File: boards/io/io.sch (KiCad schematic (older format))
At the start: 129 parts, among them J1 61304021021, J2 SSW-120-02-G-D-RA, J3 Conn_01x09, J4 Barrel_Jack_Switch, J5 Conn_01x09, J6 SSW-120-02-G-D-RA, Q1 Q_NMOS_DGS, U1 SN74ACT32PWR, U10 74HC151, U11 MC74AC273DTR2G, U12 74LS32, U13 CY62256NLL-55ZXI, U14 74LS32, U2 74LS30, U3 74ACT00MTCX, U4 AT28C256-PLCC32, U5 CY62256NLL-55ZXI, U6 SSW-116-01-T-S, U7 MC74AC273DTR2G, U8 SN74ACT244PW, U9 74LS30

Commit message: IO board: device refs and datasheet links
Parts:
- removed Q1: Q_NMOS_DGS, symbol Device:Q_NMOS_DGS
- added Q1: 2N7002, Package_TO_SOT_SMD:SOT-23, symbol Device:Q_NMOS_GSD
- J4: value Barrel_Jack_Switch -> 694106301002
- U10: value 74HC151 -> MC74HC151ADTR2G; footprint (none) -> Package_SO:TSSOP-16_4.4x5mm_P0.65mm
- U12, U14: value 74LS32 -> SN74ACT32PWR; footprint (none) -> Package_SO:TSSOP-14_4.4x5mm_P0.65mm
- U13, U5: value CY62256NLL-55ZXI -> IS61C256AL-12TLI
- U2, U9: value 74LS30 -> 74HC30D; footprint (none) -> Package_SO:SOIC-14_3.9x8.7mm_P1.27mm
- gave numbers to parts that had none: 20

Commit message: Make n_rdy an open-drain pull-up
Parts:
- removed C13: 0.1u, Capacitor_SMD:C_0805_2012Metric, symbol Device:C
- removed Q1: 2N7002, Package_TO_SOT_SMD:SOT-23, symbol Device:Q_NMOS_GSD
- removed U2: 74HC30D, Package_SO:SOIC-14_3.9x8.7mm_P1.27mm, symbol 74xx:74LS30
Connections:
- wire segments 150 -> 142
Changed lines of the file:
@@
 NoConn ~ 8650 14450
 NoConn ~ 3900 7950
-$Comp
-L 74xx:74LS30 U2
-U 1 1 603249A4
-P 15500 9450
-F 0 "U2" H 15500 9975 50  0000 C CNN
-F 1 "74HC30D" H 15500 9884 50  0000 C CNN
-F 2 "Package_SO:SOIC-14_3.9x8.7mm_P1.27mm" H 15500 9450 50  0001 C CNN
-F 3 "https://assets.nexperia.com/documents/data-sheet/74HC_HCT30.pdf" H 15500 9450 50  0001 C CNN
-	1    15500 9450
-	1    0    0    -1
-$EndComp
-$Comp
-L 74xx:74LS30 U2
-U 2 1 60326108
-P 7100 14100
-F 0 "U2" H 7330 14146 50  0000 L CNN
-F 1 "74HC30D" H 7330 14055 50  0000 L CNN
-F 2 "Package_SO:SOIC-14_3.9x8.7mm_P1.27mm" H 7100 14100 50  0001 C CNN
-F 3 "https://assets.nexperia.com/documents/data-sheet/74HC_HCT30.pdf" H 7100 14100 50  0001 C CNN
-	2    7100 14100
-	1    0    0    -1
-$EndComp
-$Comp
-L power:GND #PWR095
-U 1 1 60326F40
-P 7100 14600
-F 0 "#PWR095" H 7100 14350 50  0001 C CNN
-F 1 "GND" H 7105 14427 50  0000 C CNN
-F 2 "" H 7100 14600 50  0001 C CNN
-F 3 "" H 7100 14600 50  0001 C CNN
-	1    7100 14600
-	1    0    0    -1
-$EndComp
-$Comp
-L power:VCC #PWR094
-U 1 1 60327344
-P 7100 13600
-F 0 "#PWR094" H 7100 13450 50  0001 C CNN
-F 1 "VCC" H 7117 13773 50  0000 C CNN
-F 2 "" H 7100 13600 50  0001 C CNN
-F 3 "" H 7100 13600 50  0001 C CNN
-	1    7100 13600
-	1    0    0    -1
-$EndComp
-Text Label 15200 9350 2    50   ~ 0
-~rom_cs
-Text Label 15200 9450 2    50   ~ 0
-~raml_cs
-Text Label 15200 9550 2    50   ~ 0
-~ramh_cs
-Text Label 15200 9650 2    50   ~ 0
-~io_cs
-$Comp
-L power:VCC #PWR0100
-U 1 1 6032E8ED
-P 15100 9050
-F 0 "#PWR0100" H 15100 8900 50  0001 C CNN
-F 1 "VCC" H 15117 9223 50  0000 C CNN
-F 2 "" H 15100 9050 50  0001 C CNN
-F 3 "" H 15100 9050 50  0001 C CNN
-	1    15100 9050
-	1    0    0    -1
-$EndComp
-Wire Wire Line
-	15200 9250 15100 9250
-Wire Wire Line
-	15100 9250 15100 9150
-Wire Wire Line
-	15200 9150 15100 9150
-Connection ~ 15100 9150
-Wire Wire Line
-	15100 9150 15100 9050
-$Comp
-L power:VCC #PWR0103
-U 1 1 60342DDE
-P 15100 9950
-F 0 "#PWR0103" H 15100 9800 50  0001 C CNN
-F 1 "VCC" H 15117 10123 50  0000 C CNN
-F 2 "" H 15100 9950 50  0001 C CNN
-F 3 "" H 15100 9950 50  0001 C CNN
-	1    15100 9950
-	-1   0    0    1
-$EndComp
-Wire Wire Line
-	15200 9750 15100 9750
-Wire Wire Line
-	15100 9750 15100 9850
-Wire Wire Line
-	15200 9850 15100 9850
-Connection ~ 15100 9850
-Wire Wire Line
-	15100 9850 15100 9950
-$Comp
-L power:GND #PWR0106
-U 1 1 6036BCCA
-P 16100 9650
-F 0 "#PWR0106" H 16100 9400 50  0001 C CNN
-F 1 "GND" H 16105 9477 50  0000 C CNN
-F 2 "" H 16100 9650 50  0001 C CNN
-F 3 "" H 16100 9650 50  0001 C CNN
-	1    16100 9650
-	1    0    0    -1
-$EndComp
-Text Label 16100 9250 2    50   ~ 0
-~rdy
 Wire Notes Line
 	16850 7350 16850 11600
@@
 	1    0    0    -1
 $EndComp
-$Comp
-L Device:C C13
-U 1 1 603D7405
-P 7150 15300
-F 0 "C13" H 7265 15346 50  0000 L CNN
-F 1 "0.1u" H 7265 15255 50  0000 L CNN
-F 2 "Capacitor_SMD:C_0805_2012Metric" H 7188 15150 50  0001 C CNN
-F 3 "~" H 7150 15300 50  0001 C CNN
-	1    7150 15300
-	1    0    0    -1
-$EndComp
-$Comp
-L power:GND #PWR0117
-U 1 1 603D740B
-P 7150 15450
-F 0 "#PWR0117" H 7150 15200 50  0001 C CNN
-F 1 "GND" H 7155 15277 50  0000 C CNN
-F 2 "" H 7150 15450 50  0001 C CNN
-F 3 "" H 7150 15450 50  0001 C CNN
-	1    7150 15450
-	1    0    0    -1
-$EndComp
-$Comp
-L power:VCC #PWR0116
-U 1 1 603D7411
-P 7150 15150
-F 0 "#PWR0116" H 7150 15000 50  0001 C CNN
-F 1 "VCC" H 7167 15323 50  0000 C CNN
-F 2 "" H 7150 15150 50  0001 C CNN
-F 3 "" H 7150 15150 50  0001 C CNN
-	1    7150 15150
-	1    0    0    -1
-$EndComp
 Wire Bus Line
 	17000 3250 17000 4100
@@
 Wire Bus Line
 	9350 1200 9350 2600
-$Comp
-L Device:Q_NMOS_GSD Q1
-U 1 1 603E8383
-P 16000 9450
-F 0 "Q1" H 16204 9496 50  0000 L CNN
-F 1 "2N7002" H 16204 9405 50  0000 L CNN
-F 2 "Package_TO_SOT_SMD:SOT-23" H 16200 9550 50  0001 C CNN
-F 3 "~" H 16000 9450 50  0001 C CNN
-	1    16000 9450
-	1    0    0    -1
-$EndComp
 $EndSCHEMATC

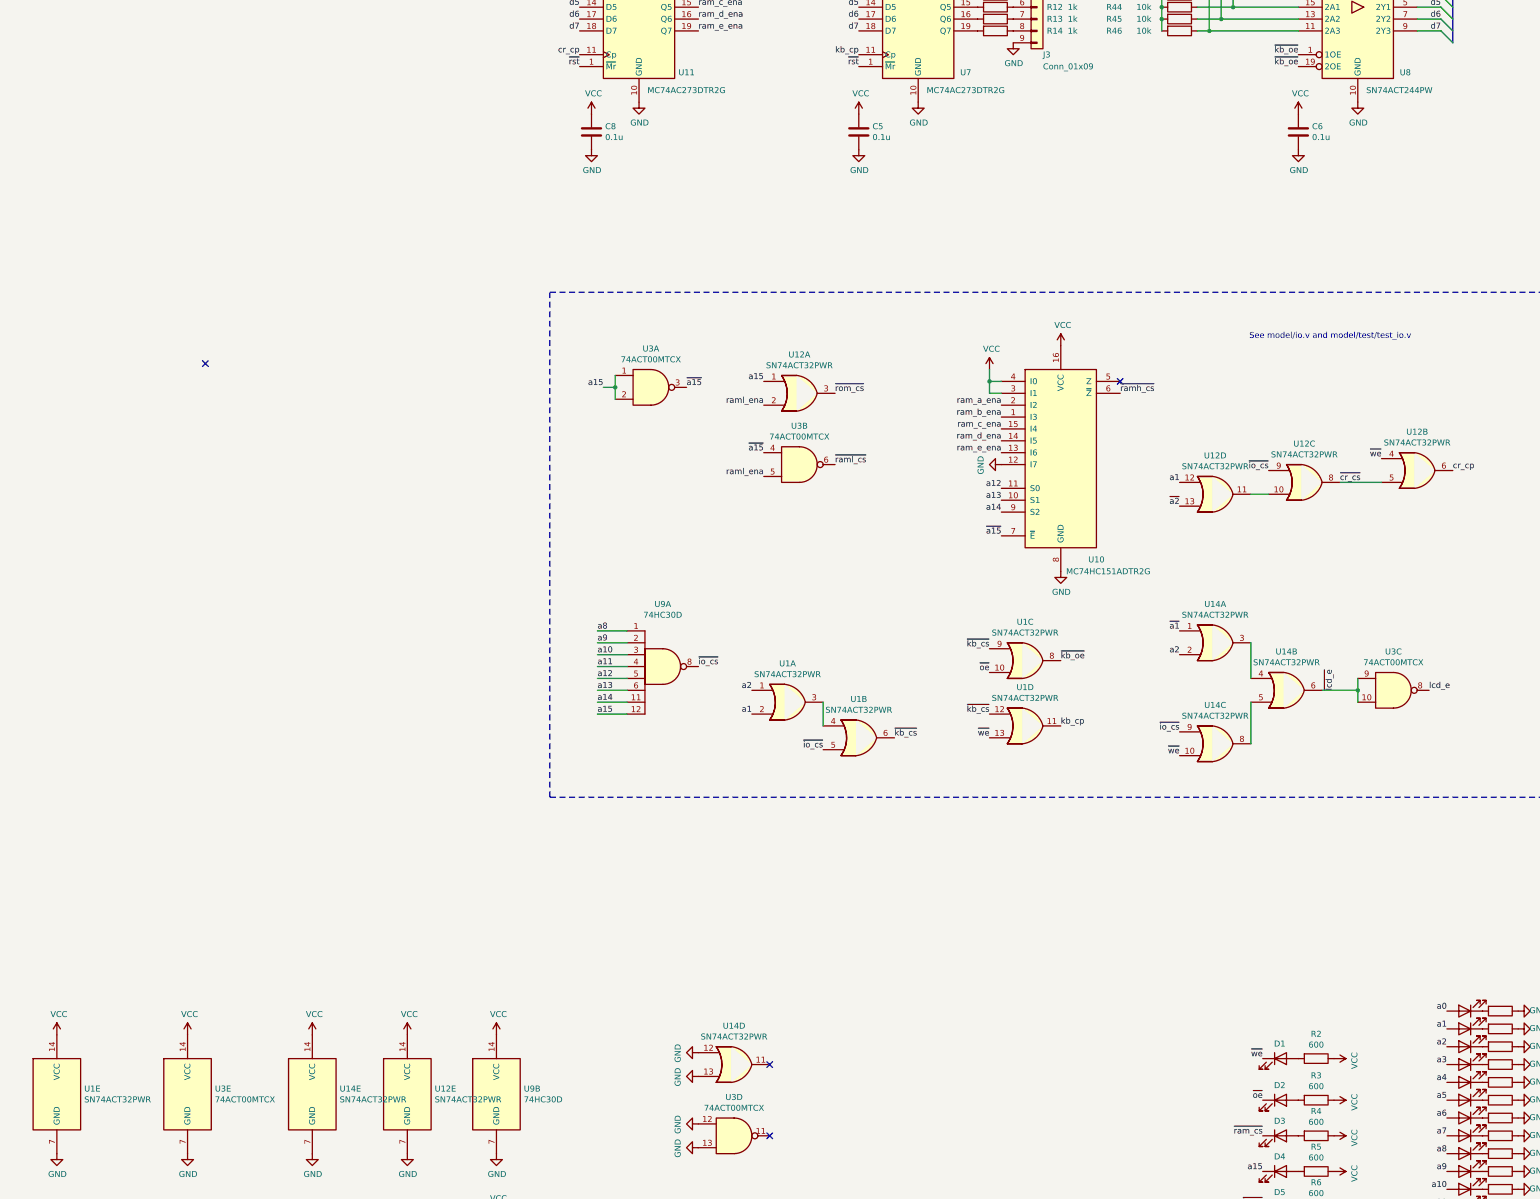
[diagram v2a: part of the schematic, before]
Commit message: IO: get rid of 74AC
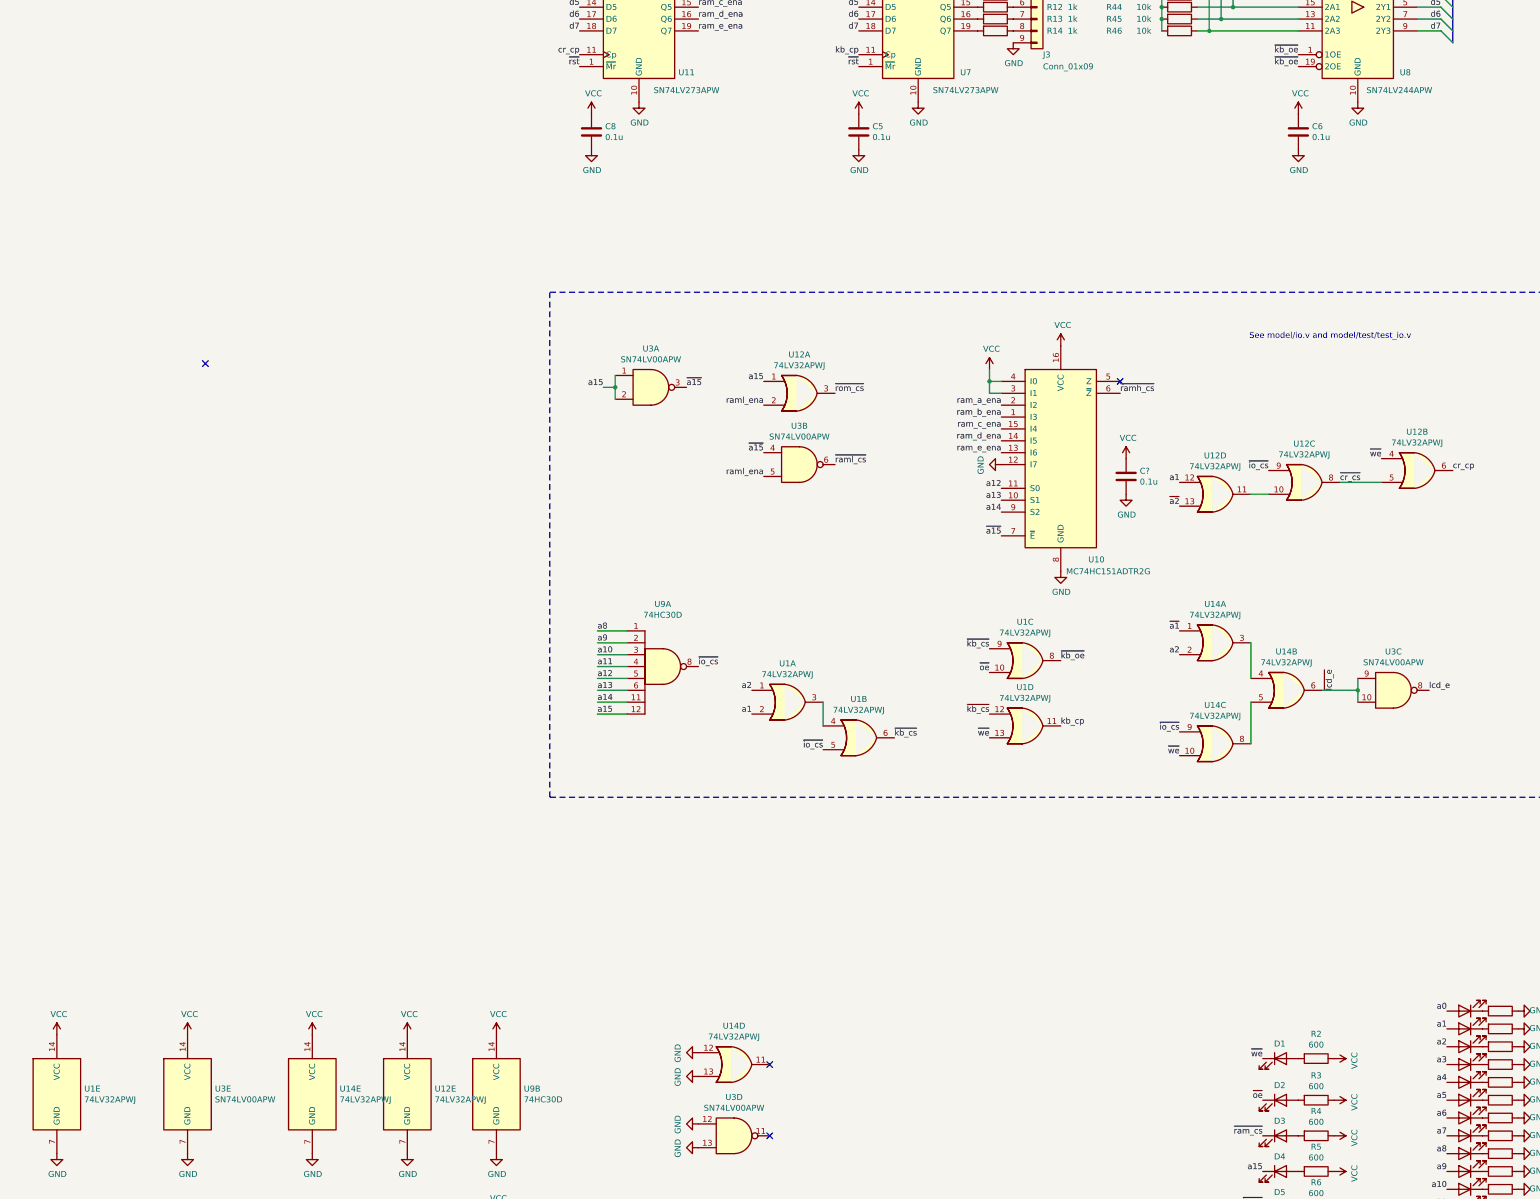
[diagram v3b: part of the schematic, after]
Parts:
- added C?: 0.1u, Capacitor_SMD:C_0805_2012Metric, symbol Device:C
- C7: footprint Capacitor_SMD:CP_Elec_4x4.5 -> Capacitor_Tantalum_SMD:CP_EIA-3528-21_Kemet-B_Pad1.50x2.35mm_HandSolder
- J3, J5: footprint (none) -> Connector_PinHeader_2.54mm:PinHeader_1x09_P2.54mm_Vertical
- U1, U12, U14: value SN74ACT32PWR -> 74LV32APWJ
- U11, U7: value MC74AC273DTR2G -> SN74LV273APW
- U3: value 74ACT00MTCX -> SN74LV00APW
- U8: value SN74ACT244PW -> SN74LV244APW
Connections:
- net GND: now also C?.2
- net VCC: now also C?.1

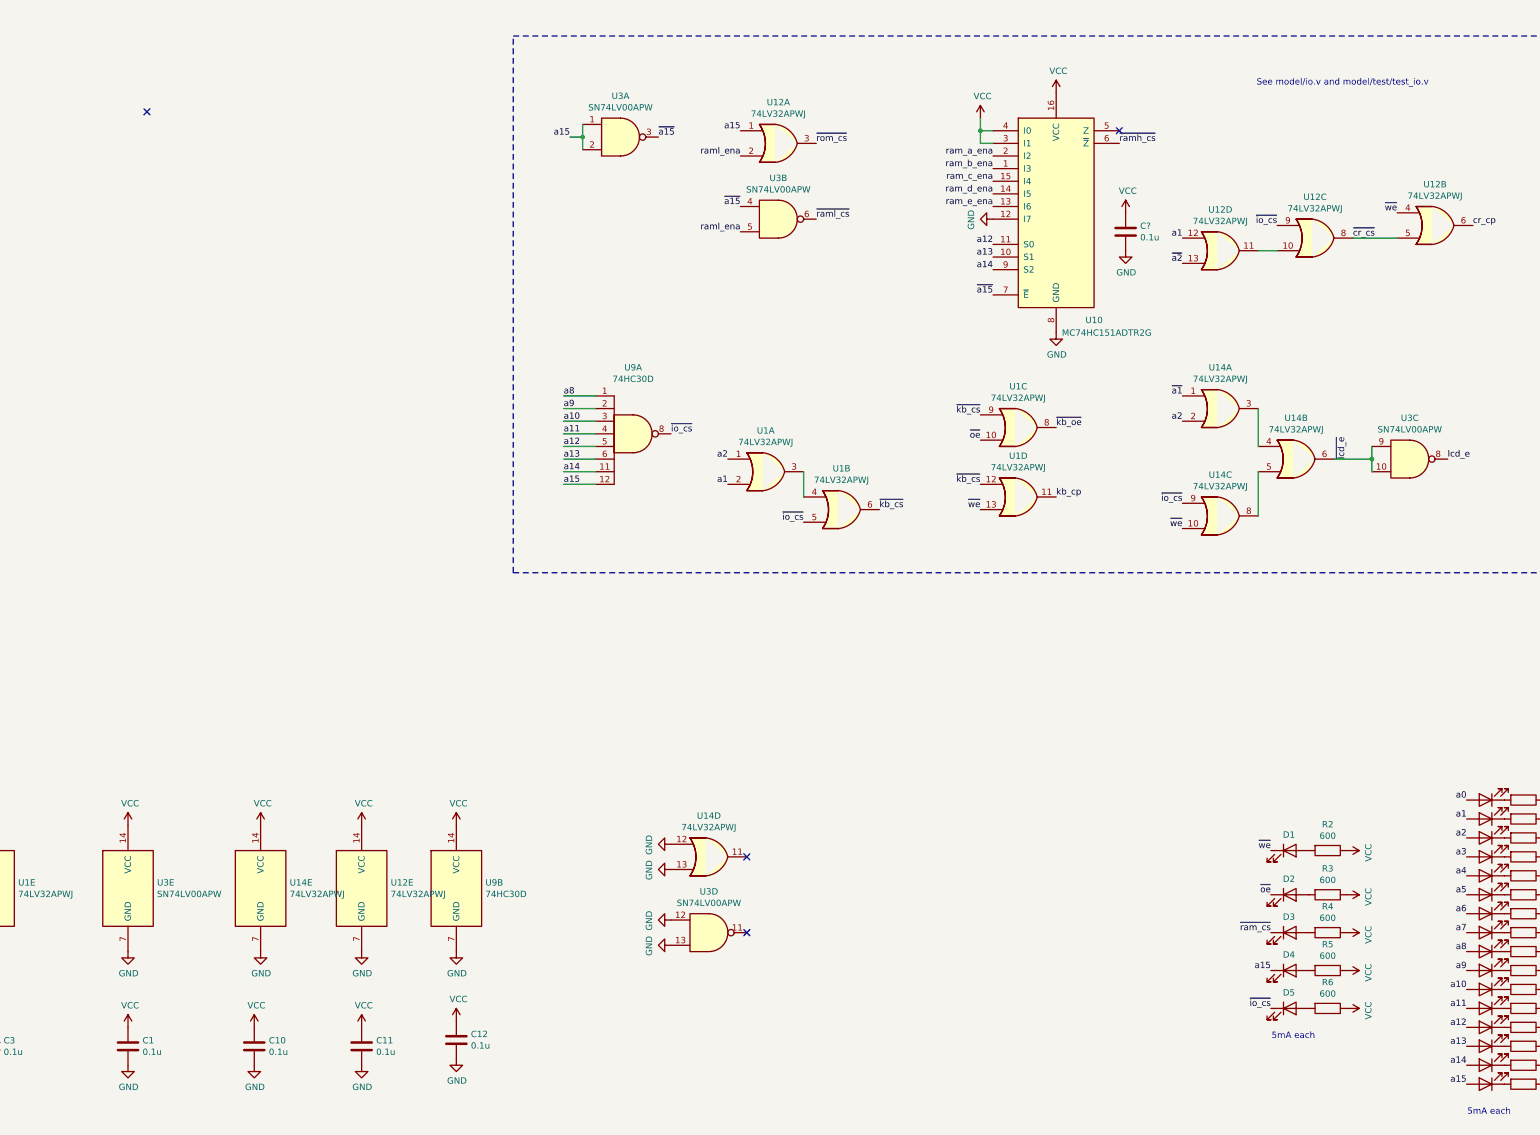
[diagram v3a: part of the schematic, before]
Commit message: IO: fix schematics according to model
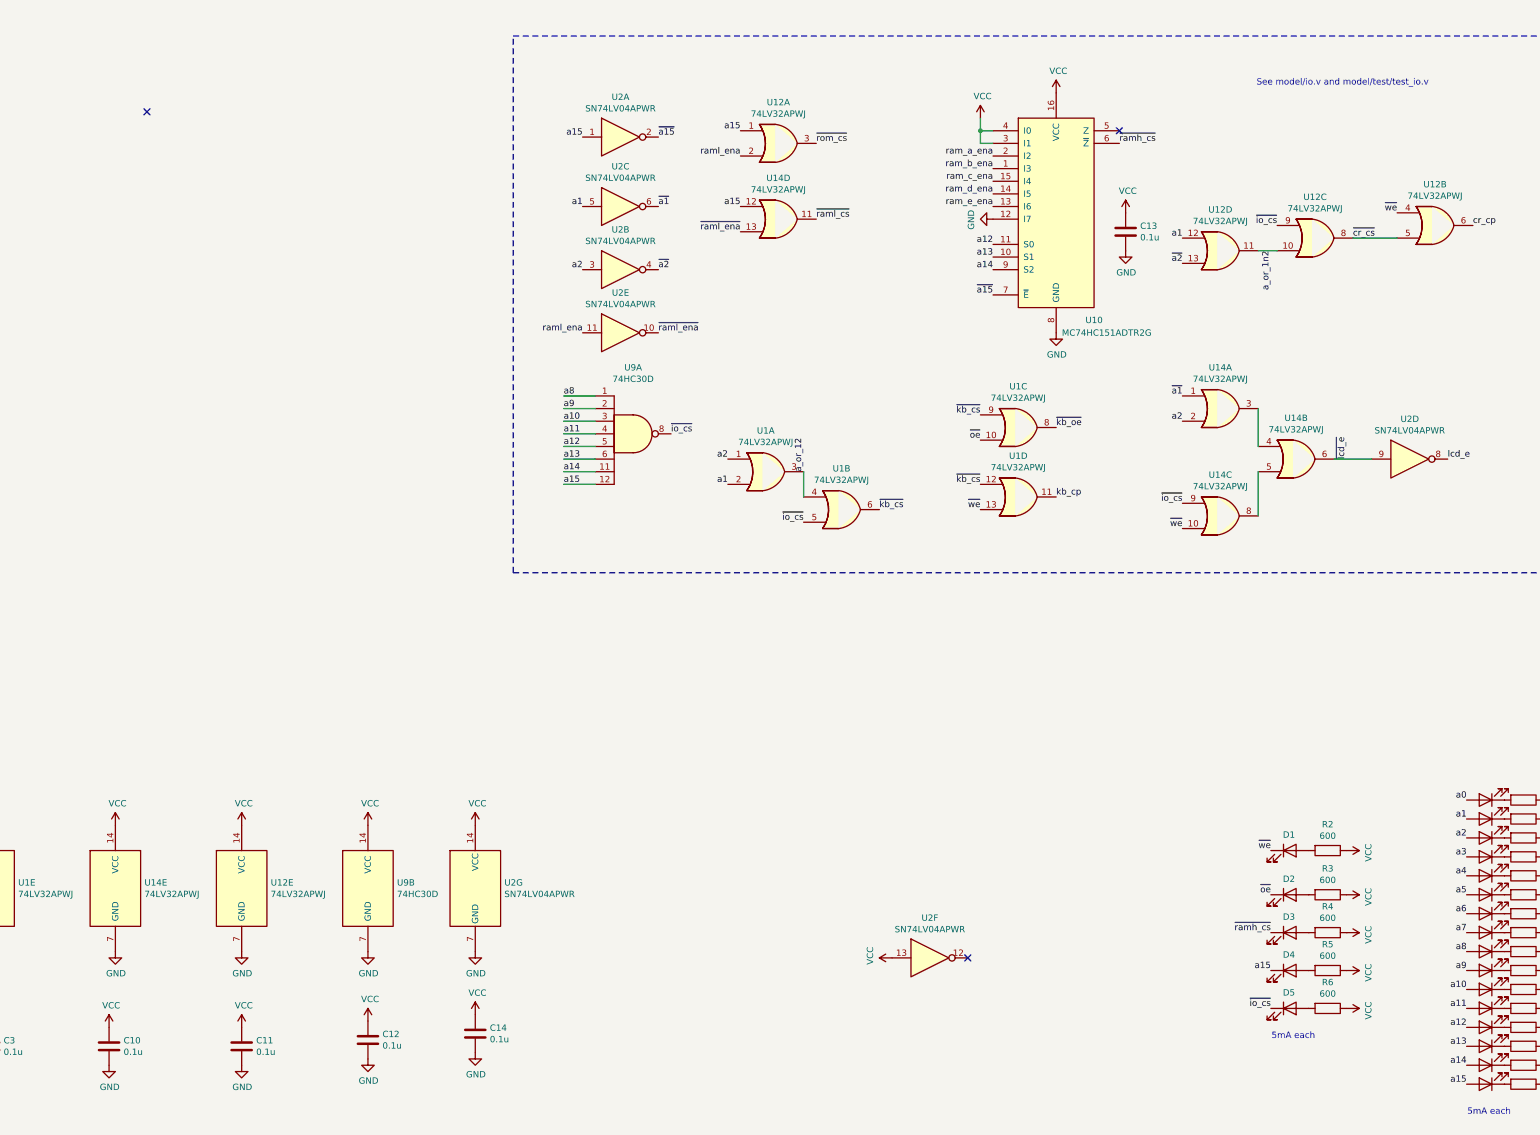
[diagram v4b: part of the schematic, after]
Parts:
- removed C1: 0.1u, Capacitor_SMD:C_0805_2012Metric, symbol Device:C
- removed U3: SN74LV00APW, Package_SO:TSSOP-14_4.4x5mm_P0.65mm, symbol 74xx:74HC00
- added C14: 0.1u, Capacitor_SMD:C_0805_2012Metric, symbol Device:C
- added U2: SN74LV04APWR, Package_SO:TSSOP-14_4.4x5mm_P0.65mm, symbol 74xx:74HC04
- gave numbers to parts that had none: 1
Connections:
- net ~ram_cs is gone; now on net ~ramh_cs: D3.1 (K)
- net GND: now also C14.2, U2.7 (GND); no longer U14.12, U14.13
- net VCC: now also C14.1, U2.13, U2.14 (VCC)
- net a1: now also U2.5
- net a15: now also U14.12, U2.1
- net a2: now also U2.3
- net lcd_e: now also U2.8
- net raml_ena: now also U2.11
- net ~a1: now also U2.6
- net ~a15: now also U2.2
- net ~a2: now also U2.4
- net ~lcd_e: now also U2.9
- net ~raml_cs: now also U14.11
- net a_or_12: now reaches U1.3, U1.4
- net a_or_1n2: now reaches U12.10, U12.11
- new net ~raml_ena: U14.13, U2.10
- no-connect marks 27 -> 26
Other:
- moved on the sheet: C10, C11, C12, U12E, U14D, U14E, U9B
